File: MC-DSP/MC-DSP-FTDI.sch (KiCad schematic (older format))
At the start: 26 parts

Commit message: updated top level of schematic with "to test" and "to do" notes
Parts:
- added D? (x2): LED, symbol Device:LED
- added R? (x2): 10K, symbol Device:R_Small
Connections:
- wire segments 110 -> 119
- no-connect marks 3 -> 6
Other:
- note removed: "ADD JTAG connector between DSP and FTDI chip\nDSP pg 110\n"
- note removed: "TODO\nLEDs\n93LC56C-I/SN"
- moved on the sheet: C?, U?

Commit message: ADC refs, FTDI changes, and more
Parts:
- removed C?: 0.1uF, symbol Device:C
- added C? (x2): 4.7uF, symbol Device:C
- added C? (x7): 0.1uF, symbol Device:C
- added D?: D_Schottky, Diode_SMD:D_SMF, symbol Device:D_Schottky
- added D?: LED, symbol Device:LED
- added R?: 1K, symbol Device:R_Small
- added U? (x3): ISO7730DW, symbol DSP_symbols:ISO7730DW
- added U?: AZ1117-3.3, Package_TO_SOT_SMD:SOT-89-3_Handsoldering, symbol Regulator_Linear:AZ1117-3.3
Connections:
- net labels added: DSP_3V3, DSP_GND, DSP_SCI-RX, DSP_SCI-TX, DSP_TCK, DSP_TDI, DSP_TDO, DSP_TMS, DSP_TRSTn, EMU_1V8, EMU_3V3, EMU_5V, EMU_GND, EMU_USB_5V
- net labels removed: +1V8, +3V3, +5V
- wire segments 119 -> 164
- no-connect marks 6 -> 16
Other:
- moved on the sheet: C?, D?, J?, L?, R?, U?

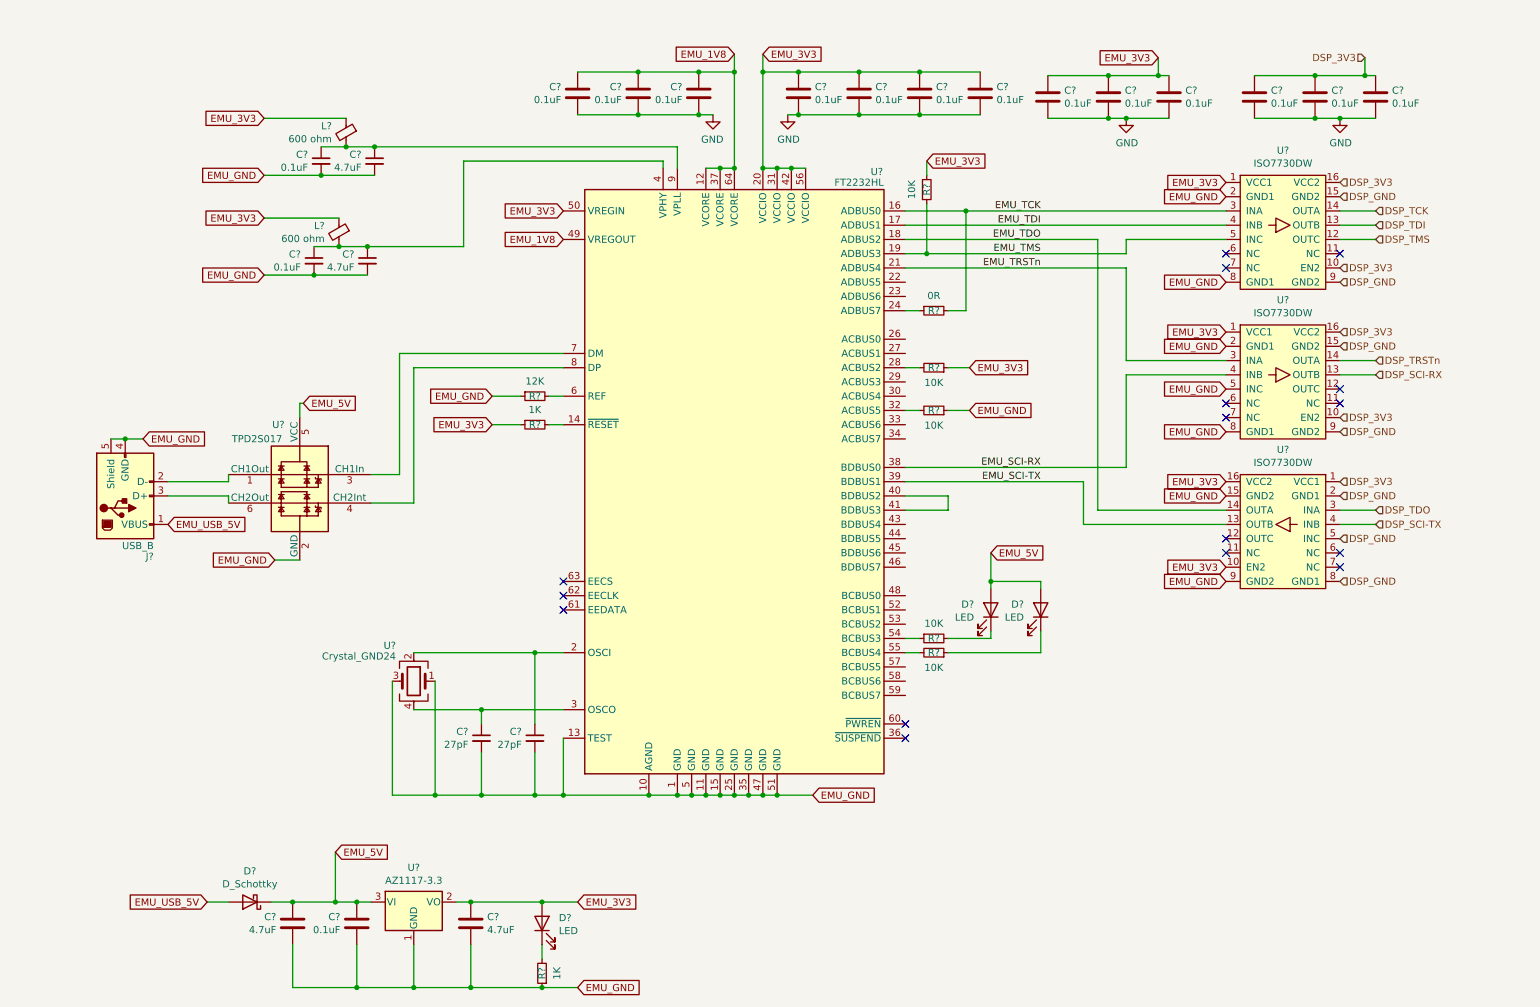
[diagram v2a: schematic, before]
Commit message: All parts labeled, just need to pick passives basically.
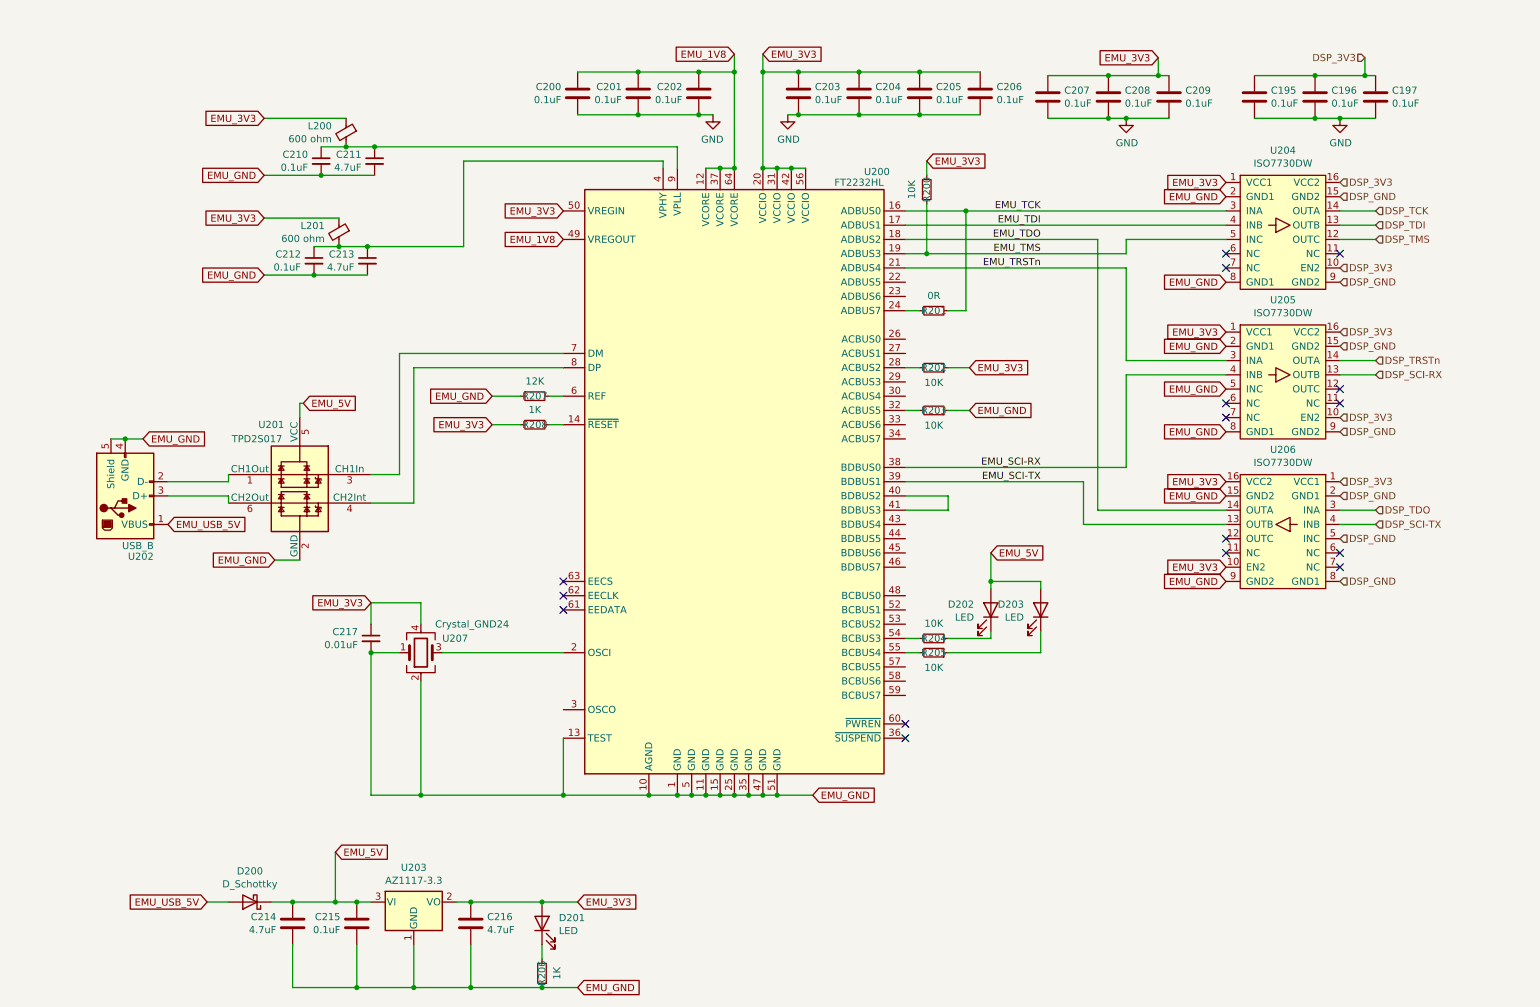
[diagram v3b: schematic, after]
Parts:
- removed C?: 27pF, symbol Device:C_Small
- C195, C196, C197, C200, C201, C202, C203, C204, C205, C206, C207, C208, C209, C210, C211, C212, C213, C214, C215, C216: renamed from C?; footprint (none) -> Capacitor_SMD:C_0201_0603Metric_Pad0.64x0.40mm_HandSolder
- C217: renamed from C?; value 27pF -> 0.01uF; footprint (none) -> Capacitor_SMD:C_0201_0603Metric_Pad0.64x0.40mm_HandSolder
- D201, D202, D203: renamed from D?; footprint (none) -> LED_THT:LED_D3.0mm
- L200, L201: renamed from L?; footprint (none) -> ?
- R200, R201, R202, R203, R204, R205, R206, R207, R208: renamed from R?; footprint (none) -> Resistor_SMD:R_0603_1608Metric_Pad0.98x0.95mm_HandSolder
- U202: renamed from J?; footprint (none) -> Connector_USB:USB_B_OST_USB-B1HSxx_Horizontal
- U204, U205, U206: renamed from U?; footprint (none) -> Package_SO:SOIC-16W_7.5x10.3mm_P1.27mm
- U207: renamed from U?; footprint (none) -> Crystal:Crystal_SMD_FOX_FQ7050-4Pin_7.0x5.0mm
- gave numbers to parts that had none: 4
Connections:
- net EMU_3V3: now also C217.1, U207.4
- net EMU_GND: now also U207.2; no longer U207.3
- net at U200.2 (OSCI): now also U207.3; no longer U207.2
- now unconnected: U200.3 (OSCO)
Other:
- moved on the sheet: C217, U207

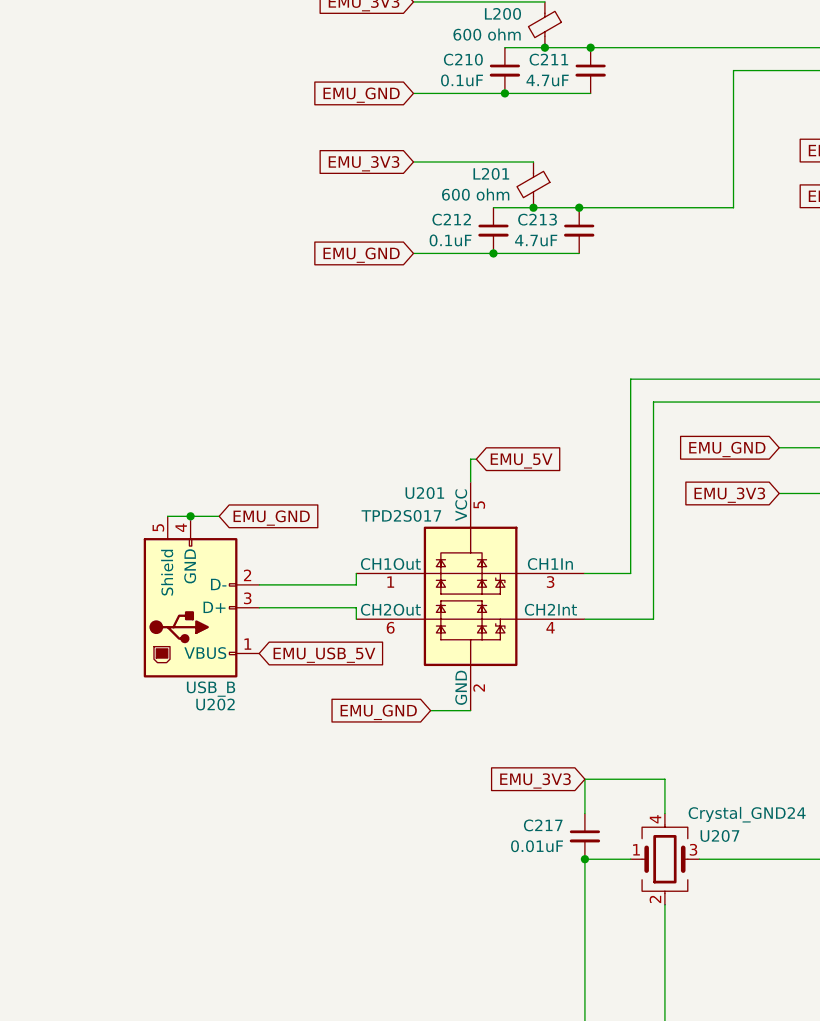
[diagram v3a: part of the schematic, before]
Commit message: DSP - added footprints and links to most parts
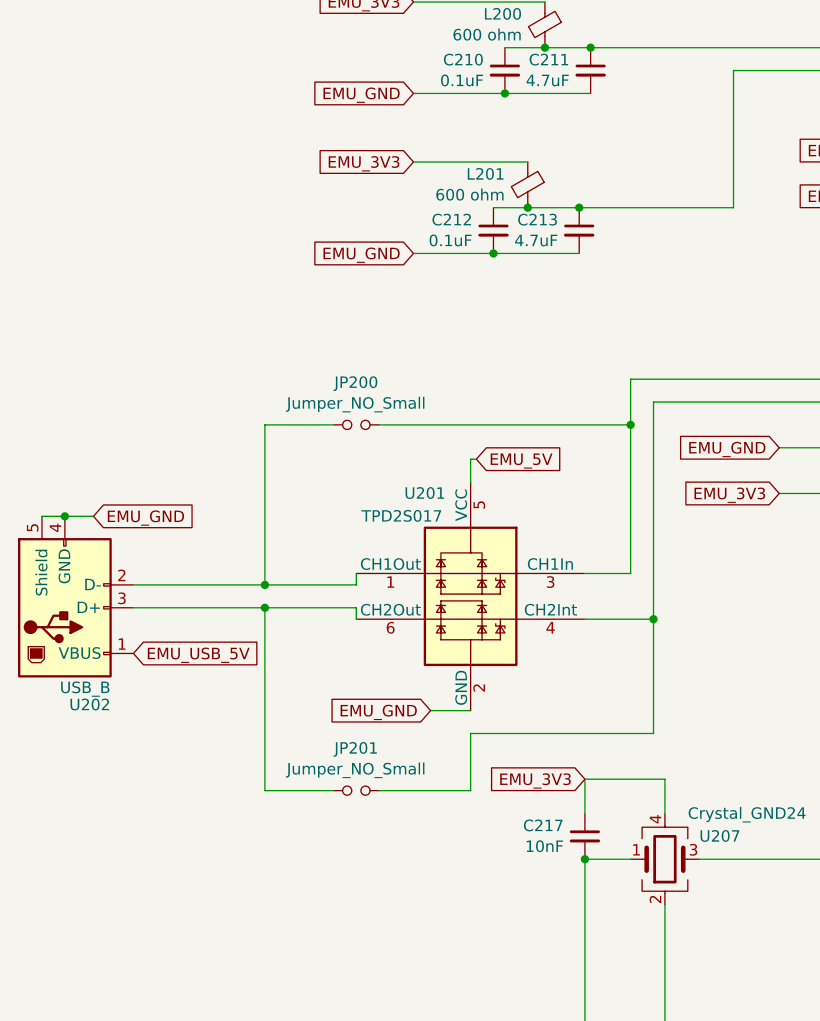
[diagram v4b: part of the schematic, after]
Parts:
- added JP200, JP201: Jumper_NO_Small, Jumper:SolderJumper-2_P1.3mm_Open_RoundedPad1.0x1.5mm, symbol Device:Jumper_NO_Small
- C217: value 0.01uF -> 10nF
- L200, L201: footprint ? -> Inductor_SMD:L_0805_2012Metric_Pad1.05x1.20mm_HandSolder
- U207: footprint Crystal:Crystal_SMD_FOX_FQ7050-4Pin_7.0x5.0mm -> ????????
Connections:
- net at U201.1 (CH1Out), U202.2 (D-): now also JP200.1
- net at U200.7 (DM), U201.3 (CH1In): now also JP200.2
- net at U200.8 (DP), U201.4 (CH2Int): now also JP201.2
- net at U201.6 (CH2Out), U202.3 (D+): now also JP201.1
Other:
- moved on the sheet: U202

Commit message: Removed clock buffer, misc leds, ethernet
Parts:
- C195, C196, C197, C200, C201, C202, C203, C204, C205, C206, C207, C208, C209, C210, C211, C212, C213, C214, C215, C216, C217: footprint Capacitor_SMD:C_0201_0603Metric_Pad0.64x0.40mm_HandSolder -> Capacitor_SMD:C_0603_1608Metric_Pad1.08x0.95mm_HandSolder
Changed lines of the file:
@@
 $Descr A4 11693 8268
 encoding utf-8
-Sheet 8 9
+Sheet 7 7
 Title ""
 Date ""
@@
 F 0 "C202" H 5565 1121 50  0000 L CNN
 F 1 "0.1uF" H 5565 1030 50  0000 L CNN
-F 2 "Capacitor_SMD:C_0201_0603Metric_Pad0.64x0.40mm_HandSolder" H 5488 925 50  0001 C CNN
+F 2 "Capacitor_SMD:C_0603_1608Metric_Pad1.08x0.95mm_HandSolder" H 5488 925 50  0001 C CNN
 F 3 "https://www.digikey.com/en/products/detail/yageo/CC0603KRX7R9BB104/2103082" H 5450 1075 50  0001 C CNN
 	1    5450 1075
@@
 F 0 "C201" H 5140 1121 50  0000 L CNN
 F 1 "0.1uF" H 5140 1030 50  0000 L CNN
-F 2 "Capacitor_SMD:C_0201_0603Metric_Pad0.64x0.40mm_HandSolder" H 5063 925 50  0001 C CNN
+F 2 "Capacitor_SMD:C_0603_1608Metric_Pad1.08x0.95mm_HandSolder" H 5063 925 50  0001 C CNN
 F 3 "https://www.digikey.com/en/products/detail/yageo/CC0603KRX7R9BB104/2103082" H 5025 1075 50  0001 C CNN
 	1    5025 1075
@@
 F 0 "C200" H 4715 1121 50  0000 L CNN
 F 1 "0.1uF" H 4715 1030 50  0000 L CNN
-F 2 "Capacitor_SMD:C_0201_0603Metric_Pad0.64x0.40mm_HandSolder" H 4638 925 50  0001 C CNN
+F 2 "Capacitor_SMD:C_0603_1608Metric_Pad1.08x0.95mm_HandSolder" H 4638 925 50  0001 C CNN
 F 3 "https://www.digikey.com/en/products/detail/yageo/CC0603KRX7R9BB104/2103082" H 4600 1075 50  0001 C CNN
 	1    4600 1075
@@
 F 0 "C203" H 6265 1121 50  0000 L CNN
 F 1 "0.1uF" H 6265 1030 50  0000 L CNN
-F 2 "Capacitor_SMD:C_0201_0603Metric_Pad0.64x0.40mm_HandSolder" H 6188 925 50  0001 C CNN
+F 2 "Capacitor_SMD:C_0603_1608Metric_Pad1.08x0.95mm_HandSolder" H 6188 925 50  0001 C CNN
 F 3 "https://www.digikey.com/en/products/detail/yageo/CC0603KRX7R9BB104/2103082" H 6150 1075 50  0001 C CNN
 	1    6150 1075
@@
 F 0 "C204" H 6690 1121 50  0000 L CNN
 F 1 "0.1uF" H 6690 1030 50  0000 L CNN
-F 2 "Capacitor_SMD:C_0201_0603Metric_Pad0.64x0.40mm_HandSolder" H 6613 925 50  0001 C CNN
+F 2 "Capacitor_SMD:C_0603_1608Metric_Pad1.08x0.95mm_HandSolder" H 6613 925 50  0001 C CNN
 F 3 "https://www.digikey.com/en/products/detail/yageo/CC0603KRX7R9BB104/2103082" H 6575 1075 50  0001 C CNN
 	1    6575 1075
@@
 F 0 "C205" H 7115 1121 50  0000 L CNN
 F 1 "0.1uF" H 7115 1030 50  0000 L CNN
-F 2 "Capacitor_SMD:C_0201_0603Metric_Pad0.64x0.40mm_HandSolder" H 7038 925 50  0001 C CNN
+F 2 "Capacitor_SMD:C_0603_1608Metric_Pad1.08x0.95mm_HandSolder" H 7038 925 50  0001 C CNN
 F 3 "https://www.digikey.com/en/products/detail/yageo/CC0603KRX7R9BB104/2103082" H 7000 1075 50  0001 C CNN
 	1    7000 1075
@@
 F 0 "C206" H 7540 1121 50  0000 L CNN
 F 1 "0.1uF" H 7540 1030 50  0000 L CNN
-F 2 "Capacitor_SMD:C_0201_0603Metric_Pad0.64x0.40mm_HandSolder" H 7463 925 50  0001 C CNN
+F 2 "Capacitor_SMD:C_0603_1608Metric_Pad1.08x0.95mm_HandSolder" H 7463 925 50  0001 C CNN
 F 3 "https://www.digikey.com/en/products/detail/yageo/CC0603KRX7R9BB104/2103082" H 7425 1075 50  0001 C CNN
 	1    7425 1075
@@
 F 0 "C211" H 3267 1596 50  0000 L CNN
 F 1 "4.7uF" H 3267 1505 50  0000 L CNN
-F 2 "Capacitor_SMD:C_0201_0603Metric_Pad0.64x0.40mm_HandSolder" H 3175 1550 50  0001 C CNN
+F 2 "Capacitor_SMD:C_0603_1608Metric_Pad1.08x0.95mm_HandSolder" H 3175 1550 50  0001 C CNN
 F 3 "https://www.digikey.com/en/products/detail/tdk-corporation/C1608X5R1V475K080AC/3648577" H 3175 1550 50  0001 C CNN
 	1    3175 1550
@@
 F 0 "C210" H 2892 1596 50  0000 L CNN
 F 1 "0.1uF" H 2892 1505 50  0000 L CNN
-F 2 "Capacitor_SMD:C_0201_0603Metric_Pad0.64x0.40mm_HandSolder" H 2800 1550 50  0001 C CNN
+F 2 "Capacitor_SMD:C_0603_1608Metric_Pad1.08x0.95mm_HandSolder" H 2800 1550 50  0001 C CNN
 F 3 "https://www.digikey.com/en/products/detail/yageo/CC0603KRX7R9BB104/2103082" H 2800 1550 50  0001 C CNN
 	1    2800 1550
@@
 F 0 "C213" H 3217 2296 50  0000 L CNN
 F 1 "4.7uF" H 3217 2205 50  0000 L CNN
-F 2 "Capacitor_SMD:C_0201_0603Metric_Pad0.64x0.40mm_HandSolder" H 3125 2250 50  0001 C CNN
+F 2 "Capacitor_SMD:C_0603_1608Metric_Pad1.08x0.95mm_HandSolder" H 3125 2250 50  0001 C CNN
 F 3 "https://www.digikey.com/en/products/detail/tdk-corporation/C1608X5R1V475K080AC/3648577" H 3125 2250 50  0001 C CNN
 	1    3125 2250
@@
 F 0 "C212" H 2842 2296 50  0000 L CNN
 F 1 "0.1uF" H 2842 2205 50  0000 L CNN
-F 2 "Capacitor_SMD:C_0201_0603Metric_Pad0.64x0.40mm_HandSolder" H 2750 2250 50  0001 C CNN
+F 2 "Capacitor_SMD:C_0603_1608Metric_Pad1.08x0.95mm_HandSolder" H 2750 2250 50  0001 C CNN
 F 3 "https://www.digikey.com/en/products/detail/yageo/CC0603KRX7R9BB104/2103082" H 2750 2250 50  0001 C CNN
 	1    2750 2250
@@
 F 0 "C216" H 3965 6946 50  0000 L CNN
 F 1 "4.7uF" H 3965 6855 50  0000 L CNN
-F 2 "Capacitor_SMD:C_0201_0603Metric_Pad0.64x0.40mm_HandSolder" H 3888 6750 50  0001 C CNN
+F 2 "Capacitor_SMD:C_0603_1608Metric_Pad1.08x0.95mm_HandSolder" H 3888 6750 50  0001 C CNN
 F 3 "https://www.digikey.com/en/products/detail/tdk-corporation/C1608X5R1V475K080AC/3648577" H 3850 6900 50  0001 C CNN
 	1    3850 6900
@@
 F 0 "C215" H 3165 6946 50  0000 L CNN
 F 1 "0.1uF" H 3165 6855 50  0000 L CNN
-F 2 "Capacitor_SMD:C_0201_0603Metric_Pad0.64x0.40mm_HandSolder" H 3088 6750 50  0001 C CNN
+F 2 "Capacitor_SMD:C_0603_1608Metric_Pad1.08x0.95mm_HandSolder" H 3088 6750 50  0001 C CNN
 F 3 "https://www.digikey.com/en/products/detail/yageo/CC0603KRX7R9BB104/2103082" H 3050 6900 50  0001 C CNN
 	1    3050 6900
@@
 F 0 "C214" H 2715 6946 50  0000 L CNN
 F 1 "4.7uF" H 2715 6855 50  0000 L CNN
-F 2 "Capacitor_SMD:C_0201_0603Metric_Pad0.64x0.40mm_HandSolder" H 2638 6750 50  0001 C CNN
+F 2 "Capacitor_SMD:C_0603_1608Metric_Pad1.08x0.95mm_HandSolder" H 2638 6750 50  0001 C CNN
 F 3 "https://www.digikey.com/en/products/detail/tdk-corporation/C1608X5R1V475K080AC/3648577" H 2600 6900 50  0001 C CNN
 	1    2600 6900
@@
 F 0 "C207" H 8015 1146 50  0000 L CNN
 F 1 "0.1uF" H 8015 1055 50  0000 L CNN
-F 2 "Capacitor_SMD:C_0201_0603Metric_Pad0.64x0.40mm_HandSolder" H 7938 950 50  0001 C CNN
+F 2 "Capacitor_SMD:C_0603_1608Metric_Pad1.08x0.95mm_HandSolder" H 7938 950 50  0001 C CNN
 F 3 "https://www.digikey.com/en/products/detail/yageo/CC0603KRX7R9BB104/2103082" H 7900 1100 50  0001 C CNN
 	1    7900 1100
@@
 F 0 "C208" H 8440 1146 50  0000 L CNN
 F 1 "0.1uF" H 8440 1055 50  0000 L CNN
-F 2 "Capacitor_SMD:C_0201_0603Metric_Pad0.64x0.40mm_HandSolder" H 8363 950 50  0001 C CNN
+F 2 "Capacitor_SMD:C_0603_1608Metric_Pad1.08x0.95mm_HandSolder" H 8363 950 50  0001 C CNN
 F 3 "https://www.digikey.com/en/products/detail/yageo/CC0603KRX7R9BB104/2103082" H 8325 1100 50  0001 C CNN
 	1    8325 1100
@@
 F 0 "C209" H 8865 1146 50  0000 L CNN
 F 1 "0.1uF" H 8865 1055 50  0000 L CNN
-F 2 "Capacitor_SMD:C_0201_0603Metric_Pad0.64x0.40mm_HandSolder" H 8788 950 50  0001 C CNN
+F 2 "Capacitor_SMD:C_0603_1608Metric_Pad1.08x0.95mm_HandSolder" H 8788 950 50  0001 C CNN
 F 3 "https://www.digikey.com/en/products/detail/yageo/CC0603KRX7R9BB104/2103082" H 8750 1100 50  0001 C CNN
 	1    8750 1100
@@
 F 0 "C195" H 9465 1146 50  0000 L CNN
 F 1 "0.1uF" H 9465 1055 50  0000 L CNN
-F 2 "Capacitor_SMD:C_0201_0603Metric_Pad0.64x0.40mm_HandSolder" H 9388 950 50  0001 C CNN
+F 2 "Capacitor_SMD:C_0603_1608Metric_Pad1.08x0.95mm_HandSolder" H 9388 950 50  0001 C CNN
 F 3 "https://www.digikey.com/en/products/detail/yageo/CC0603KRX7R9BB104/2103082" H 9350 1100 50  0001 C CNN
 	1    9350 1100
@@
 F 0 "C196" H 9890 1146 50  0000 L CNN
 F 1 "0.1uF" H 9890 1055 50  0000 L CNN
-F 2 "Capacitor_SMD:C_0201_0603Metric_Pad0.64x0.40mm_HandSolder" H 9813 950 50  0001 C CNN
+F 2 "Capacitor_SMD:C_0603_1608Metric_Pad1.08x0.95mm_HandSolder" H 9813 950 50  0001 C CNN
 F 3 "https://www.digikey.com/en/products/detail/yageo/CC0603KRX7R9BB104/2103082" H 9775 1100 50  0001 C CNN
 	1    9775 1100
@@
 F 0 "C197" H 10315 1146 50  0000 L CNN
 F 1 "0.1uF" H 10315 1055 50  0000 L CNN
-F 2 "Capacitor_SMD:C_0201_0603Metric_Pad0.64x0.40mm_HandSolder" H 10238 950 50  0001 C CNN
+F 2 "Capacitor_SMD:C_0603_1608Metric_Pad1.08x0.95mm_HandSolder" H 10238 950 50  0001 C CNN
 F 3 "https://www.digikey.com/en/products/detail/yageo/CC0603KRX7R9BB104/2103082" H 10200 1100 50  0001 C CNN
 	1    10200 1100
@@
 F 0 "C217" H 3242 4946 50  0000 L CNN
 F 1 "10nF" H 3242 4855 50  0000 L CNN
-F 2 "Capacitor_SMD:C_0201_0603Metric_Pad0.64x0.40mm_HandSolder" H 3150 4900 50  0001 C CNN
+F 2 "Capacitor_SMD:C_0603_1608Metric_Pad1.08x0.95mm_HandSolder" H 3150 4900 50  0001 C CNN
 F 3 "https://www.digikey.com/en/products/detail/kemet/C0603X103J4HAC7867/8334457" H 3150 4900 50  0001 C CNN
 	1    3150 4900
